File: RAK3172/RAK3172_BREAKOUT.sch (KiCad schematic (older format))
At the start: 4 parts, among them J1 Conn_01x14_Male, J2 Conn_01x14_Male, J3 Conn_01x14_Male, U1 RAK3712

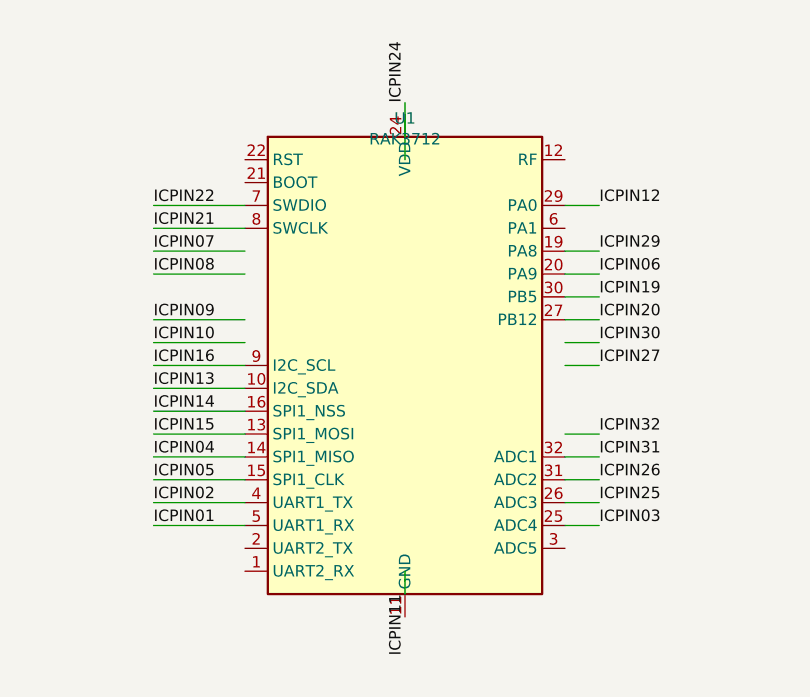
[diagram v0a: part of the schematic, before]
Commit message: proj:(DIL_BREAKOUT_PCB RAK 3712)changed project filenames
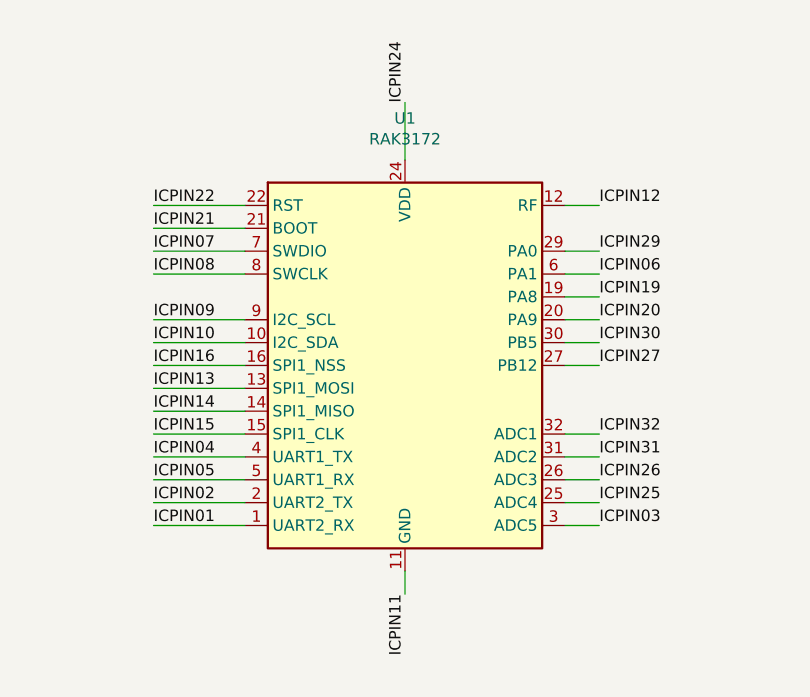
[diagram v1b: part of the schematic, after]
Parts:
- removed U1: RAK3712, RAKWIRELESS:RAK3712, symbol RAKWIRELESS:RAK3712
- added U1: RAK3172, RAKWIRELESS:RAK3172, symbol RAKWIRELESS:RAK3172
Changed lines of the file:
@@
 encoding utf-8
 Sheet 1 1
-Title "RAK3712_BREAKOUT"
+Title "RAK3172_BREAKOUT"
 Date ""
 Rev ""
@@
 Text Label 6500 3150 0    50   ~ 0
 ICPIN32
-$Comp
-L RAKWIRELESS:RAK3712 U1
-U 1 1 621FE0F5
-P 5650 2850
-F 0 "U1" H 5650 3931 50  0000 C CNN
-F 1 "RAK3712" H 5650 3840 50  0000 C CNN
-F 2 "RAKWIRELESS:RAK3712" H 5850 3150 50  0001 C CNN
-F 3 "https://site-file.fomillesite.com/1260815565112336386/1427562149389201410.pdf" H 5850 3150 50  0001 C CNN
-	1    5650 2850
-	1    0    0    -1
-$EndComp
 $Comp
 L Connector:Conn_01x14_Male J1
@@
 Wire Wire Line
 	9000 3550 9550 3550
+$Comp
+L RAKWIRELESS:RAK3172 U1
+U 1 1 621FD6BE
+P 5650 2850
+F 0 "U1" H 5650 3931 50  0000 C CNN
+F 1 "RAK3172" H 5650 3840 50  0000 C CNN
+F 2 "RAKWIRELESS:RAK3172" H 5850 3150 50  0001 C CNN
+F 3 "https://site-file.fomillesite.com/1260815565112336386/1427562149389201410.pdf" H 5850 3150 50  0001 C CNN
+	1    5650 2850
+	1    0    0    -1
+$EndComp
 $EndSCHEMATC
